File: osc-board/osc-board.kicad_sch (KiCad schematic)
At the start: 68 parts, among them J1 01x20, J2 01x20, Q1 MMBT3906, Q2 MMBT3906, SW1 SW_DIP_x02, SW2 SW_DIP_x02, U1 LM13700, U2 TL074, U3 TL074

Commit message: wip pre-redo orientation
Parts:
- removed C5, C7: 1u, Capacitor_SMD:C_0603_1608Metric_Pad1.08x0.95mm_HandSolder, symbol Device:C
- removed C6, C8: 100n, Capacitor_SMD:C_0603_1608Metric_Pad1.08x0.95mm_HandSolder, symbol Device:C
- removed SW1, SW2: SW_DIP_x02, Button_Switch_SMD:SW_DIP_SPSTx02_Slide_Omron_A6S-210x_W8.9mm_P2.54mm, symbol Switch:SW_DIP_x02
- added J3, J4: Conn_01x03_Female, Connector_PinHeader_2.54mm:PinHeader_1x03_P2.54mm_Vertical, symbol Connector:Conn_01x03_Female
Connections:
- net +4.5V: now also U1.14 (+), U1.3 (+), U3.5 (+), J3.2 (Pin_2), J4.2 (Pin_2); no longer U1.14 (+), U1.3 (+), U3.10 (+)
- net Osc1_Iabc: now also U1.1; no longer U1.16
- net Osc1_Integr_In: now also U1.5, J3.1 (Pin_1); no longer U1.12
- net Osc1_Integr_Out: now also J3.3 (Pin_3)
- net Osc2_Iabc: now also U1.16; no longer U1.1
- net Osc2_Integr_In: now also U1.12, U3.6 (-), J4.1 (Pin_1); no longer U1.5, U3.9 (-)
- net Osc2_Integr_Out: now also U3.7, J4.3 (Pin_3); no longer U3.8
- net at R1.1, R3.1: now also U1.4 (-); no longer U1.13 (-)
- net at R32.2, R34.2: now also U3.10 (+); no longer U3.5 (+)
- net at R30.1, R31.1: now also U3.9 (-); no longer U3.6 (-)
- net at R36.1: now also U3.8; no longer U3.7
- net at R2.1, R4.1: now also U1.13 (-); no longer U1.4 (-)

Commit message: wip
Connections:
- net +4.5V: now also U2.12 (+); no longer U2.3 (+)
- net Osc1_FB: now also U2.7; no longer U2.14
- net at Q1.1 (B): now also U2.14; no longer U2.1
- net at R18.2, R21.1: now also U2.5 (+); no longer U2.12 (+)
- net at R17.2: now also U2.6 (-); no longer U2.13 (-)
- net at R35.1: now also U2.1; no longer U2.7
- net at C1.1, R5.2, R6.2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: now also U2.13 (-); no longer U2.2 (-)
- net at R29.2, R33.2: now also U2.3 (+); no longer U2.5 (+)
- net at R27.1, R28.1: now also U2.2 (-); no longer U2.6 (-)
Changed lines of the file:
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@@
     (pin "6")
   )
-  (symbol (lib_id "Amplifier_Operational:TL074") (at 140.97 78.74 0) (mirror x) (unit 4)
+  (symbol (lib_id "Amplifier_Operational:TL074") (at 140.97 78.74 0) (mirror x) (unit 2)
     (in_bom yes) (on_board yes) (fields_autoplaced)
     (property "Reference" "U2" (id 0) (at 140.97 68.58 0))
@@
     (pin "2")
   )
-  (symbol (lib_id "Amplifier_Operational:TL074") (at 213.36 78.74 0) (mirror x) (unit 2)
+  (symbol (lib_id "Amplifier_Operational:TL074") (at 213.36 78.74 0) (mirror x) (unit 1)
     (in_bom yes) (on_board yes) (fields_autoplaced)
     (property "Reference" "U2" (id 0) (at 213.36 68.58 0))
@@
     )
   )
-  (symbol (lib_id "Amplifier_Operational:TL074") (at 54.61 46.99 0) (mirror x) (unit 1)
+  (symbol (lib_id "Amplifier_Operational:TL074") (at 54.61 46.99 0) (mirror x) (unit 4)
     (in_bom yes) (on_board yes) (fields_autoplaced)
     (property "Reference" "U2" (id 0) (at 54.61 36.83 0))
@@
       (reference "U1") (unit 5) (value "LM13700") (footprint "Package_SO:SOP-16_4.55x10.3mm_P1.27mm")
     )
-    (path "/c9b601fe-ff4c-4a1f-8701-896a8f230020"
+    (path "/c8b8aed9-b344-4140-9a17-9b7636e9756e"
       (reference "U2") (unit 1) (value "TL074") (footprint "Package_SO:SOIC-14_3.9x8.7mm_P1.27mm")
     )
-    (path "/c8b8aed9-b344-4140-9a17-9b7636e9756e"
+    (path "/1b833b28-a746-4445-8a15-87f4027cbc1b"
       (reference "U2") (unit 2) (value "TL074") (footprint "Package_SO:SOIC-14_3.9x8.7mm_P1.27mm")
     )
@@
       (reference "U2") (unit 3) (value "TL074") (footprint "Package_SO:SOIC-14_3.9x8.7mm_P1.27mm")
     )
-    (path "/1b833b28-a746-4445-8a15-87f4027cbc1b"
+    (path "/c9b601fe-ff4c-4a1f-8701-896a8f230020"
       (reference "U2") (unit 4) (value "TL074") (footprint "Package_SO:SOIC-14_3.9x8.7mm_P1.27mm")
     )

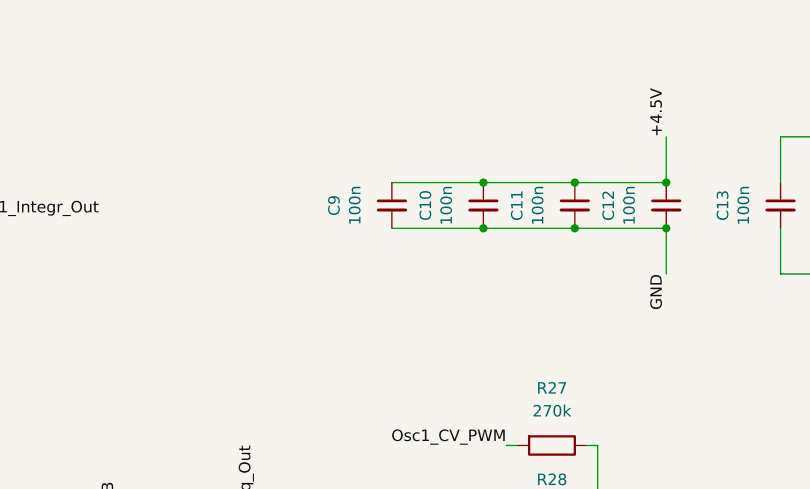
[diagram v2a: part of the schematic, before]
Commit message: OSC board layout done
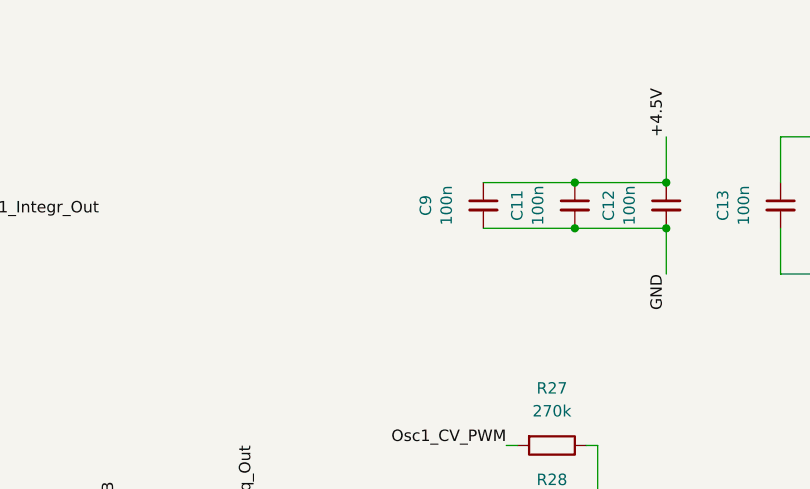
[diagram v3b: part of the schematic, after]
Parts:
- removed C10: 100n, Capacitor_SMD:C_0603_1608Metric_Pad1.08x0.95mm_HandSolder, symbol Device:C_Small
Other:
- moved on the sheet: C9
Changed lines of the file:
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@@
   (junction (at 148.59 175.26) (diameter 0) (color 0 0 0 0)
   )
-  (junction (at 193.04 30.48) (diameter 0) (color 0 0 0 0)
-  )
   (junction (at 85.09 102.87) (diameter 0) (color 0 0 0 0)
   )
@@
   )
   (junction (at 205.74 134.62) (diameter 0) (color 0 0 0 0)
-  )
-  (junction (at 193.04 35.56) (diameter 0) (color 0 0 0 0)
   )
   (junction (at 205.74 81.28) (diameter 0) (color 0 0 0 0)
@@
     (stroke (width 0) (type default) (color 0 0 0 0))
   )
-  (wire (pts (xy 182.88 30.48) (xy 193.04 30.48))
-    (stroke (width 0) (type default) (color 0 0 0 0))
-  )
   (wire (pts (xy 148.59 78.74) (xy 148.59 91.44))
     (stroke (width 0) (type default) (color 0 0 0 0))
@@
   )
   (wire (pts (xy 90.17 172.72) (xy 90.17 161.29))
-    (stroke (width 0) (type default) (color 0 0 0 0))
-  )
-  (wire (pts (xy 182.88 35.56) (xy 193.04 35.56))
     (stroke (width 0) (type default) (color 0 0 0 0))
   )
@@
     (pin "2")
   )
-  (symbol (lib_id "Device:C_Small") (at 193.04 33.02 0) (unit 1)
-    (in_bom yes) (on_board yes)
-    (property "Reference" "C10" (id 0) (at 186.6392 33.02 90))
-    (property "Value" "100n" (id 1) (at 188.9506 33.02 90))
-    (property "Footprint" "Capacitor_SMD:C_0603_1608Metric_Pad1.08x0.95mm_HandSolder" (id 2) (at 194.0052 36.83 0)
-      (effects (font (size 1.27 1.27)) hide)
-    )
-    (property "Datasheet" "~" (id 3) (at 193.04 33.02 0)
-      (effects (font (size 1.27 1.27)) hide)
-    )
-    (property "LCSC" "C14663" (id 4) (at 193.04 33.02 0)
-      (effects (font (size 1.27 1.27)) hide)
-    )
-    (property "Role" "" (id 5) (at 193.04 33.02 0)
-      (effects (font (size 1.27 1.27)) hide)
-    )
-    (property "Mouser" "80-C0603C104M5RAUTO" (id 6) (at 193.04 33.02 0)
-      (effects (font (size 1.27 1.27)) hide)
-    )
-    (pin "1")
-    (pin "2")
-  )
   (symbol (lib_id "Device:C") (at 60.96 120.65 90) (unit 1)
     (in_bom yes) (on_board yes)
@@
     (pin "2")
   )
-  (symbol (lib_id "Device:C_Small") (at 182.88 33.02 0) (unit 1)
+  (symbol (lib_id "Device:C_Small") (at 193.04 33.02 0) (unit 1)
     (in_bom yes) (on_board yes)
-    (property "Reference" "C9" (id 0) (at 176.4792 33.02 90))
-    (property "Value" "100n" (id 1) (at 178.7906 33.02 90))
-    (property "Footprint" "Capacitor_SMD:C_0603_1608Metric_Pad1.08x0.95mm_HandSolder" (id 2) (at 183.8452 36.83 0)
-      (effects (font (size 1.27 1.27)) hide)
-    )
-    (property "Datasheet" "~" (id 3) (at 182.88 33.02 0)
-      (effects (font (size 1.27 1.27)) hide)
-    )
-    (property "LCSC" "C14663" (id 4) (at 182.88 33.02 0)
-      (effects (font (size 1.27 1.27)) hide)
-    )
-    (property "Role" "" (id 5) (at 182.88 33.02 0)
-      (effects (font (size 1.27 1.27)) hide)
-    )
-    (property "Mouser" "80-C0603C104M5RAUTO" (id 6) (at 182.88 33.02 0)
+    (property "Reference" "C9" (id 0) (at 186.6392 33.02 90))
+    (property "Value" "100n" (id 1) (at 188.9506 33.02 90))
+    (property "Footprint" "Capacitor_SMD:C_0603_1608Metric_Pad1.08x0.95mm_HandSolder" (id 2) (at 194.0052 36.83 0)
+      (effects (font (size 1.27 1.27)) hide)
+    )
+    (property "Datasheet" "~" (id 3) (at 193.04 33.02 0)
+      (effects (font (size 1.27 1.27)) hide)
+    )
+    (property "LCSC" "C14663" (id 4) (at 193.04 33.02 0)
+      (effects (font (size 1.27 1.27)) hide)
+    )
+    (property "Role" "" (id 5) (at 193.04 33.02 0)
+      (effects (font (size 1.27 1.27)) hide)
+    )
+    (property "Mouser" "80-C0603C104M5RAUTO" (id 6) (at 193.04 33.02 0)
       (effects (font (size 1.27 1.27)) hide)
     )
@@
       (reference "C9") (unit 1) (value "100n") (footprint "Capacitor_SMD:C_0603_1608Metric_Pad1.08x0.95mm_HandSolder")
     )
-    (path "/7c988018-a462-4046-b646-5bf59464c0d1"
-      (reference "C10") (unit 1) (value "100n") (footprint "Capacitor_SMD:C_0603_1608Metric_Pad1.08x0.95mm_HandSolder")
-    )
     (path "/c12bbc4f-2c21-42bc-8dce-3889bc268def"

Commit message: Carrier ordered
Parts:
- C1, C2: Mouser (none) -> 581-0603YC101KAT2A
- C3, C4: Mouser (none) -> 77-VJ0603Y223JXJAC
- Q1, Q2: Mouser (none) -> 637-MMBT3906
- R1, R10, R17, R18, R19, R2, R20, R21, R22, R28, R31, R33, R34, R5, R6, R7, R8, R9: Mouser (none) -> 71-RCS0603100KFKEA
- R11, R12, R15, R16: Mouser (none) -> 755-ESR03EZPF1001
- R13, R14: Mouser (none) -> 279-CRGP0603F680R
- R23, R24, R29, R32, R35, R36: Mouser (none) -> 279-CRGP0603F10K
- R25, R26, R37, R38: Mouser (none) -> 279-CRGP0603F8K2
- R27, R30: Mouser (none) -> 279-CRGP0603F270K
- R3, R4: Mouser (none) -> 652-CMP0603-FX-3300L
- RV1, RV2: Mouser (none) -> 652-3314J-2-104E
- U1: Mouser (none) -> 926-LM13700M/NOPB
- U2, U3: Mouser (none) -> 595-TL074IDR
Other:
- company: (none) -> Andrey Salomatin / Pedal Markt
- title: (none) -> Carrier

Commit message: Carrier: notes after testing
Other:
- note added: "After testing. Replacing R9 with 10k and shorting the other leg of R6 to 9V gives better results."
- note added: "Maybe increase R5 slightly to avoid the osc switching off at min CV but sometimes it works w/ 100k :/"
- note added: "Might make sense to expose the Osc_Integrator pins to the main header"
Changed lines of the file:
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@@
     (stroke (width 0) (type default) (color 0 0 0 0))
+  )
+  (text "After testing. Replacing R9 with 10k and\nshorting the other leg of R6 to 9V\ngives better results."
+    (at 16.51 22.86 0)
+    (effects (font (size 1 1)) (justify left bottom))
+  )
+  (text "Maybe increase R5 slightly\nto avoid the osc switching off\nat min CV\nbut sometimes it works w/ 100k :/"
+    (at 16.51 62.23 0)
+    (effects (font (size 1 1)) (justify left bottom))
+  )
+  (text "Might make sense to expose\nthe Osc_Integrator pins\nto the main header"
+    (at 144.78 26.67 0)
+    (effects (font (size 1 1)) (justify left bottom))
   )
   (label "Osc2_PWM_Out" (at 236.22 135.89 90)

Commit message: wip
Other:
- note added: "Maybe increase R5 slightly (to 120k) to avoid the osc switching off at min CV but sometimes it works w/ 100k :/"
- note removed: "Maybe increase R5 slightly to avoid the osc switching off at min CV but sometimes it works w/ 100k :/"
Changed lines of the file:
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@@
     (effects (font (size 1 1)) (justify left bottom))
   )
-  (text "Maybe increase R5 slightly\nto avoid the osc switching off\nat min CV\nbut sometimes it works w/ 100k :/"
+  (text "Maybe increase R5 slightly (to 120k)\nto avoid the osc switching off\nat min CV\nbut sometimes it works w/ 100k :/"
     (at 16.51 62.23 0)
     (effects (font (size 1 1)) (justify left bottom))
